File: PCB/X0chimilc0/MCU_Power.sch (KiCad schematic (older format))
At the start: 53 parts

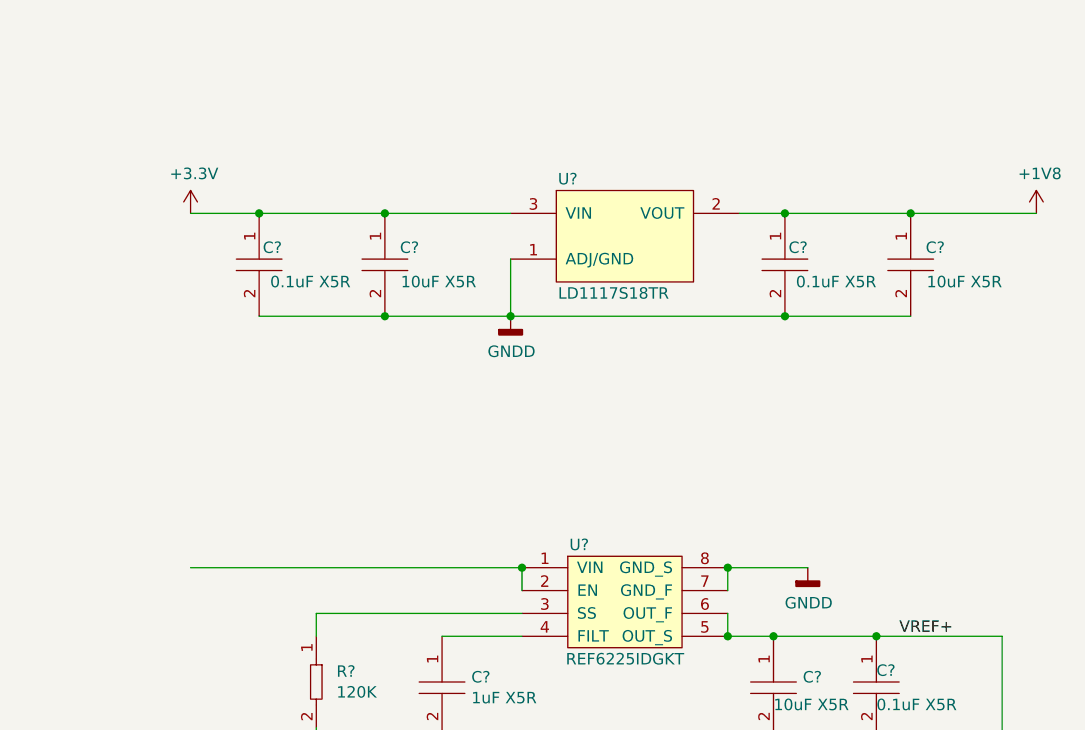
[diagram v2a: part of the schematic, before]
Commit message: Power Supply
Worked on power supply design adn schematic, still need a few more rails.
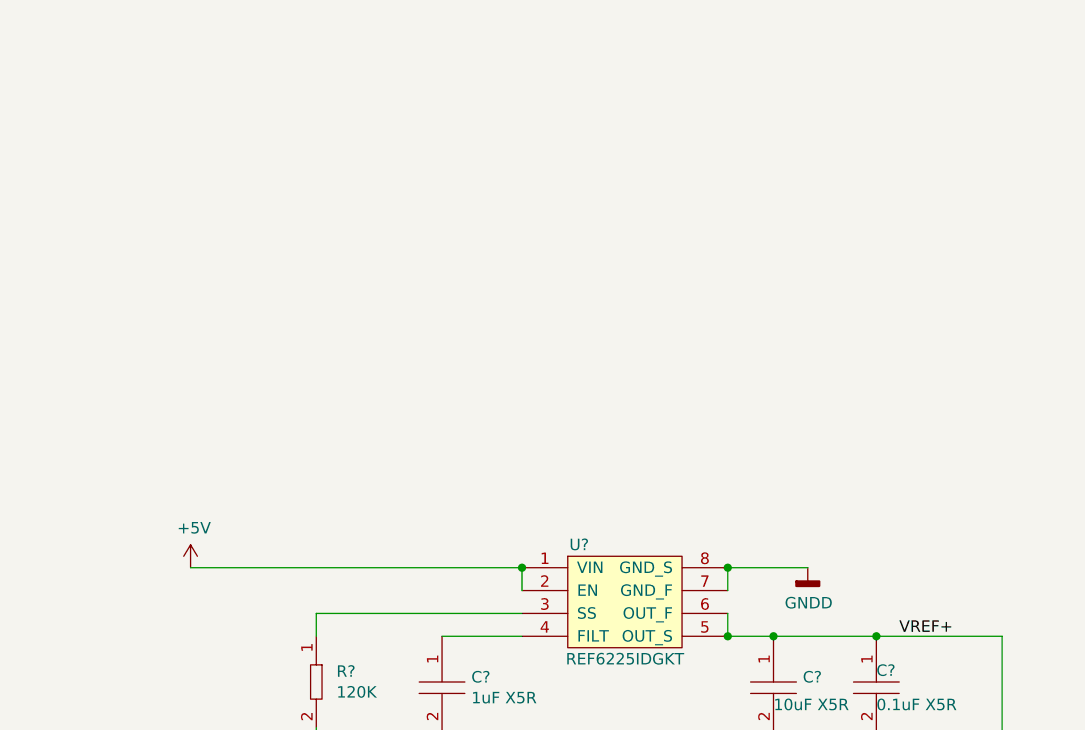
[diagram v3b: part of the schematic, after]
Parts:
- removed C? (x2): GRM188R61A106KE69D, AVR-KiCAD-Lib-Capacitors:C0603, symbol AVR-KiCAD-Lib-Capacitors:GRM188R61A106KE69D
- removed C? (x2): C0402C104K9PACTU, AVR-KiCAD-Lib-Resistors:R0402, symbol AVR-KiCAD-Lib-Capacitors:C0402C104K9PACTU
- removed U?: LD1117S18TR, AVR-KiCAD-Lib-ICs:LD1117S50TR, symbol AVR-KiCAD-Lib-ICs:LD1117S18TR
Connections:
- net +5V: now reaches U?.1 (VIN), U?.2 (EN)
